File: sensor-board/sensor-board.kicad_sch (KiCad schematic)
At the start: 103 parts, among them J1 USB_C_Receptacle_USB2.0_16P, J10 cap4, J11 header pins, J2 aux pwr, J3 SWD, J4 water 1, J5 water 2, J6 relay, J7 cap1, J8 cap2, J9 cap3, K1 SIL03-1A72-71D, Q1 Si2312, Q2 Si2312, SW1 SW_Push, U1 MLPF-WB55-01E3, U10 EKMB130711, U11 DRV5032, U2 STM32WB55CCUx, U3 MCP1703Ax-300xxTT, U4 SHT40-AD1F-R2, U5 VL53L1CXV0FY1, U6 TLV4082, U7 CLS16D24-44, U8 LIS2DE12TR, U9 FDC2114RGHR, Y1 32.768KHz, Y2 32MHz

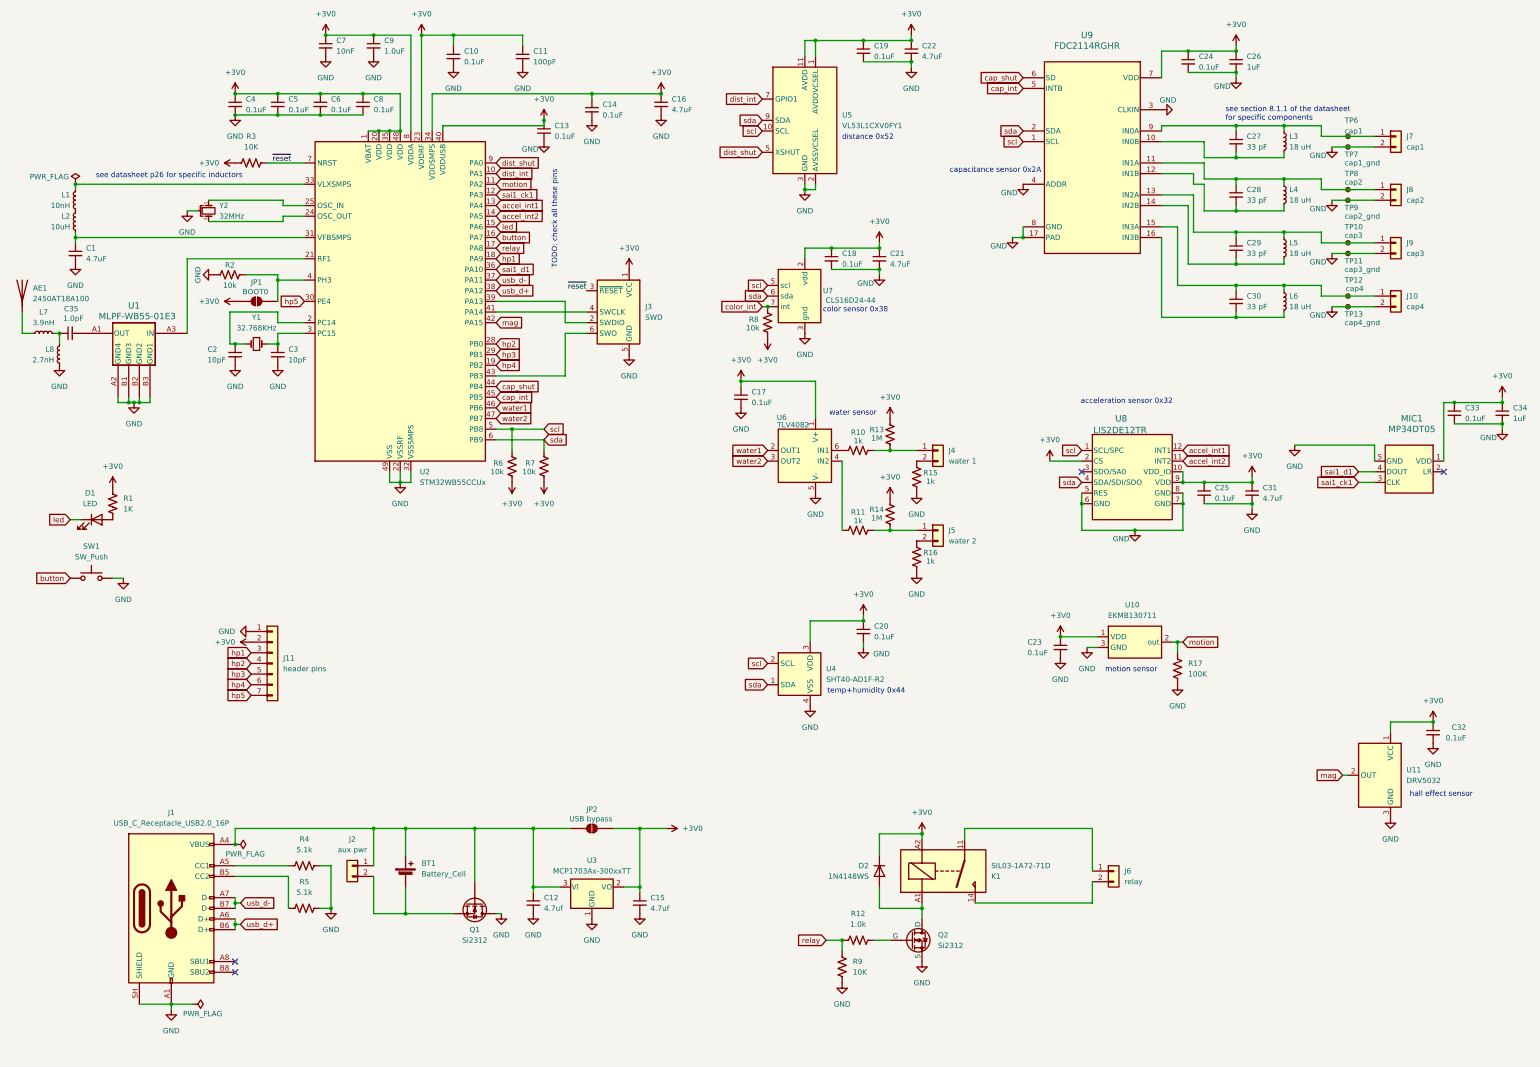
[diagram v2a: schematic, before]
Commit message: Some board grouping, no traces yet
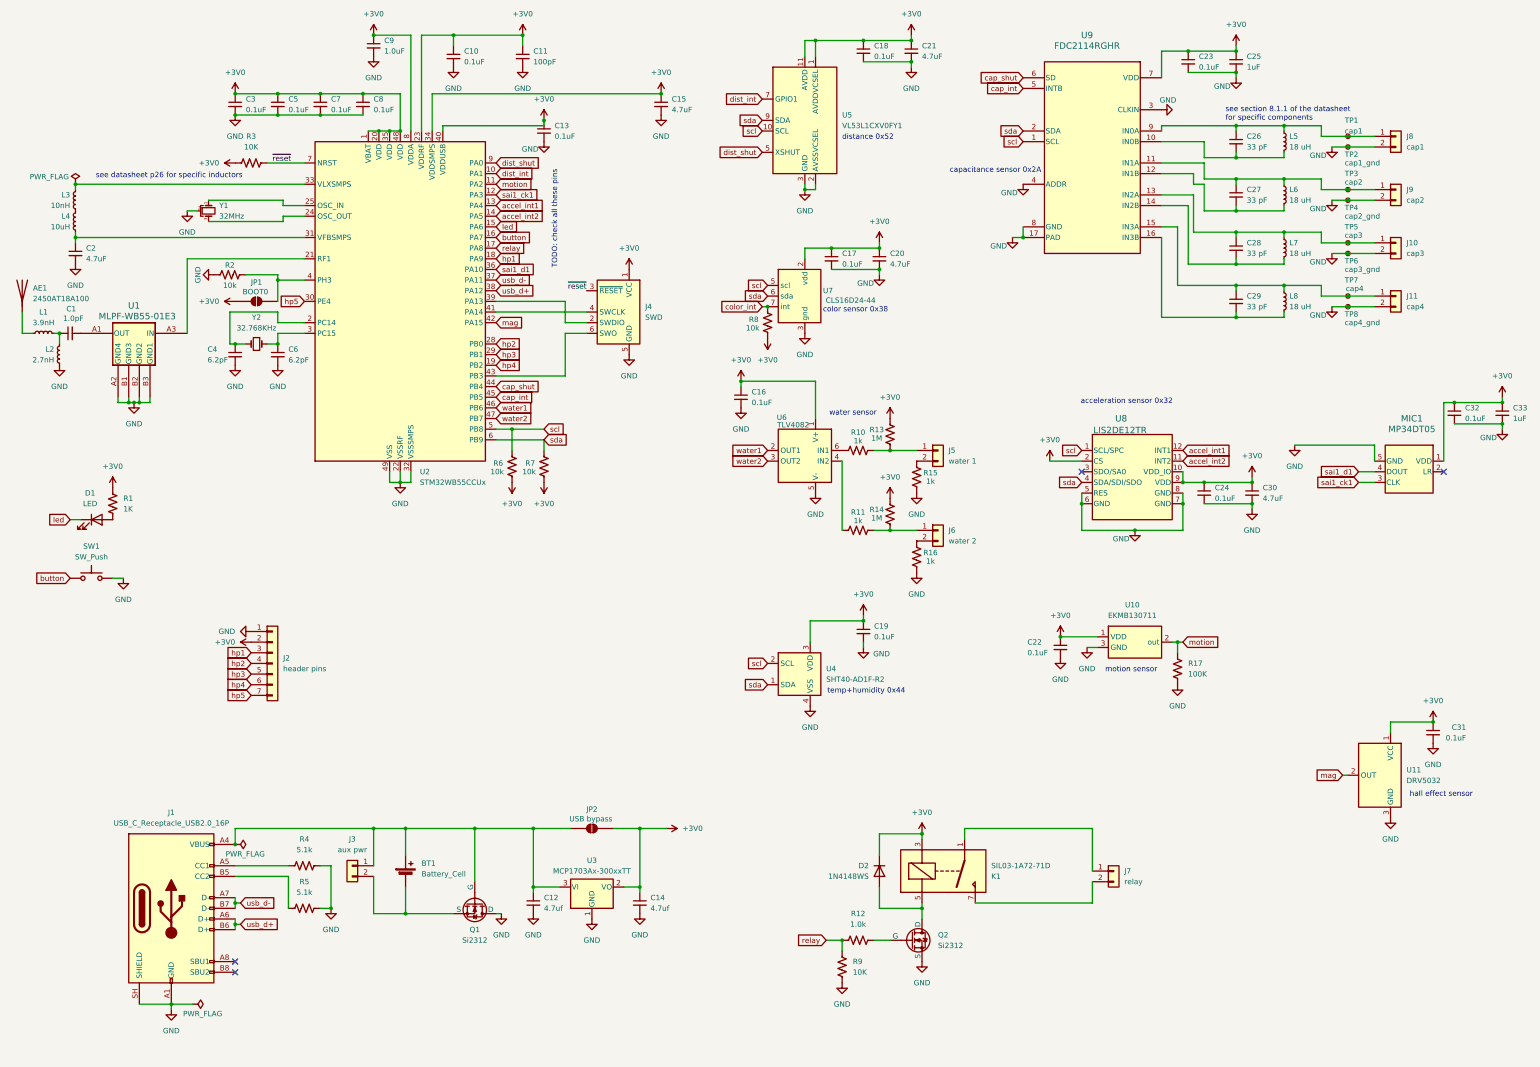
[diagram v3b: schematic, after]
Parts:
- removed C14: 0.1uF, Capacitor_SMD:C_0402_1005Metric, symbol Device:C_Small
- removed C7: 10nF, Capacitor_SMD:C_0402_1005Metric, symbol Device:C_Small
- removed Q1: Si2312, Package_TO_SOT_SMD:SOT-23, symbol Device:Q_NMOS
- added Q1: Si2312, Package_TO_SOT_SMD:SOT-23, symbol Simulation_SPICE:NMOS
- C4: renamed from C2; value 10pF -> 6.2pF
- C6: renamed from C3; value 10pF -> 6.2pF
- renumbered C35 to C1, C15 to C14, C16 to C15, C17 to C16, C18 to C17, C19 to C18, C20 to C19, C1 to C2, C21 to C20, C22 to C21, C23 to C22, C24 to C23, C25 to C24, C26 to C25, C27 to C26, C28 to C27, C29 to C28, C30 to C29, C4 to C3, C31 to C30, C32 to C31, C33 to C32, C34 to C33, C6 to C7, J9 to J10, J10 to J11, J11 to J2, J2 to J3, J3 to J4, J4 to J5, J5 to J6, J6 to J7, J7 to J8, J8 to J9, L7 to L1, L8 to L2, L1 to L3, L2 to L4, L3 to L5, L4 to L6, L5 to L7, L6 to L8, TP6 to TP1, TP7 to TP2, TP8 to TP3, TP9 to TP4, TP10 to TP5, TP11 to TP6, TP12 to TP7, TP13 to TP8, Y2 to Y1, Y1 to Y2
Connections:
- net +3V0: now also K1.3; no longer K1.A2
- net GND: now also Q1.1 (D)
- net at BT1.1 (+), C12.1, J1.A4 (VBUS)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: now also Q1.2 (G)
- net at D2.2 (A), Q2.1 (D): now also K1.5; no longer K1.A1
- net at J7.1 (Pin_1): now also K1.1; no longer K1.11
- net at J7.2 (Pin_2): now also K1.7; no longer K1.14
- net at BT1.2 (-), J3.2 (Pin_2): now also Q1.3 (S)

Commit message: Starting a little bit of routing; starting with HF crystal
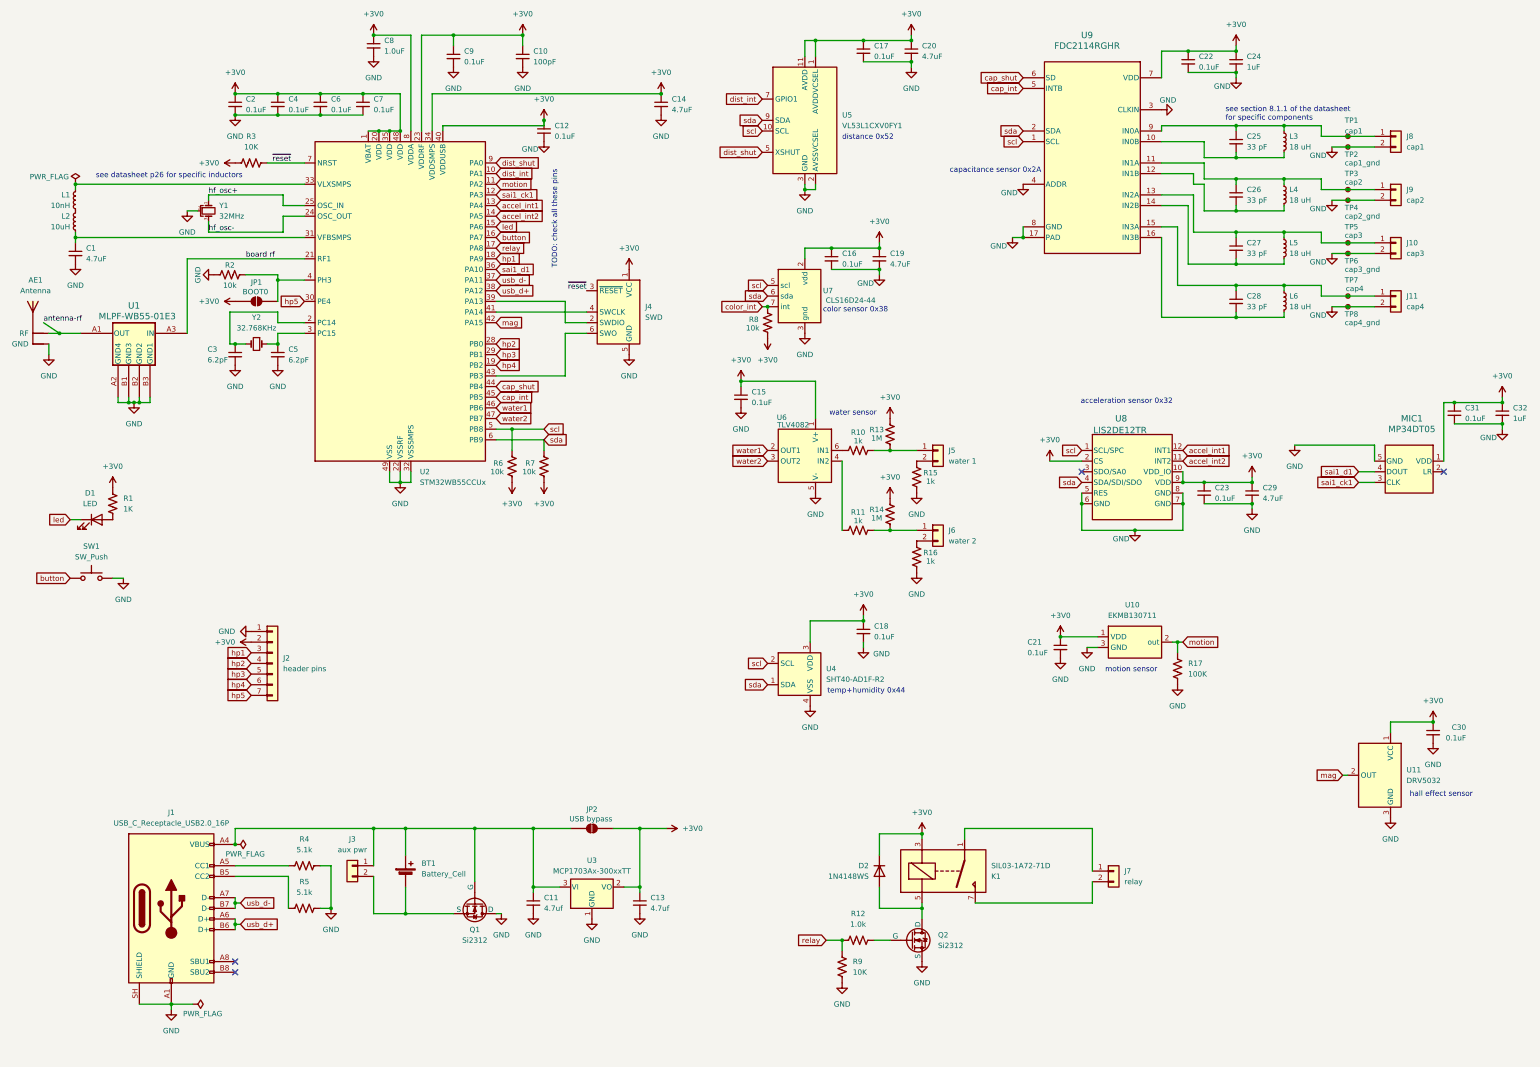
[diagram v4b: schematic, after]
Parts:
- removed C1: 1.0pF, Capacitor_SMD:C_0402_1005Metric, symbol Device:C_Small
- removed L1: 3.9nH, Inductor_SMD:L_0402_1005Metric, symbol Device:L_Small
- removed L2: 2.7nH, Inductor_SMD:L_0402_1005Metric, symbol Device:L_Small
- AE1: value 2450AT18A100 -> Antenna; footprint vendor:XDCR_ACAG0801-2450-T -> vendor:Antenna_2.4GHz_InvertedF_SiLabs; symbol Device:Antenna -> vendor:Antenna_InvertedF
- BT1: footprint (none) -> vendor:BatteryHolder_CR2032
- renumbered C2 to C1, C11 to C10, C12 to C11, C13 to C12, C14 to C13, C15 to C14, C16 to C15, C17 to C16, C18 to C17, C19 to C18, C20 to C19, C3 to C2, C21 to C20, C22 to C21, C23 to C22, C24 to C23, C25 to C24, C26 to C25, C27 to C26, C28 to C27, C29 to C28, C30 to C29, C4 to C3, C31 to C30, C32 to C31, C33 to C32, C5 to C4, C6 to C5, C7 to C6, C8 to C7, C9 to C8, C10 to C9, L3 to L1, L4 to L2, L5 to L3, L6 to L4, L7 to L5, L8 to L6
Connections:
- net GND: now also AE1.2 (GND)
- net antenna-rf: now reaches U1.A1 (OUT)
- net antenna-rf: now also AE1.1 (RF)
- net board rf: now reaches U1.A3 (IN), U2.21 (RF1)
- net hf_osc-: now reaches U2.24 (OSC_OUT), Y1.3
- net hf_osc+: now reaches U2.25 (OSC_IN), Y1.1

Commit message: SMPS and (most of) LF crystal
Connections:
- net lf_osc-: now reaches C5.1, U2.3 (PC15), Y2.1
- net lf_osc+: now reaches C3.1, U2.2 (PC14), Y2.2
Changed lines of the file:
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@@
 	)
 	(junction
-		(at 29.21 54.61)
-		(diameter 0)
-		(color 0 0 0 0)
-	)
-	(junction
 		(at 306.07 73.66)
 		(diameter 0)
@@
 	)
 	(junction
+		(at 29.21 54.61)
+		(diameter 0)
+		(color 0 0 0 0)
+	)
+	(junction
 		(at 332.74 43.18)
 		(diameter 0)
@@
 	(wire
 		(pts
+			(xy 29.21 52.07) (xy 29.21 54.61)
+		)
+		(stroke
+			(width 0)
+			(type default)
+		)
+	)
+	(wire
+		(pts
 			(xy 29.21 68.58) (xy 29.21 67.31)
 		)
@@
 		)
 	)
+	(label "lf_osc+"
+		(at 77.47 87.63 0)
+		(effects
+			(font
+				(size 1.27 1.27)
+			)
+			(justify left bottom)
+		)
+	)
 	(label "~{reset}"
 		(at 76.2 49.53 0)
@@
 		)
 	)
+	(label "lf_osc-"
+		(at 77.47 90.17 0)
+		(effects
+			(font
+				(size 1.27 1.27)
+			)
+			(justify left bottom)
+		)
+	)
 	(global_label "hp4"
 		(shape input)
@@
 	(symbol
 		(lib_id "power:PWR_FLAG")
-		(at 29.21 54.61 0)
+		(at 29.21 52.07 0)
 		(unit 1)
 		(body_style 1)
@@
 		(dnp no)
 		(property "Reference" "#FLG01"
-			(at 29.21 52.705 0)
+			(at 29.21 50.165 0)
 			(hide yes)
 			(show_name no)
@@
 		)
 		(property "Value" "PWR_FLAG"
-			(at 18.288 52.832 0)
+			(at 18.288 50.292 0)
 			(show_name no)
 			(do_not_autoplace no)
@@
 		)
 		(property "Footprint" ""
-			(at 29.21 54.61 0)
+			(at 29.21 52.07 0)
 			(hide yes)
 			(show_name no)
@@
 		)
 		(property "Datasheet" ""
-			(at 29.21 54.61 0)
+			(at 29.21 52.07 0)
 			(hide yes)
 			(show_name no)
@@
 		)
 		(property "Description" "Special symbol for telling ERC where power comes from"
-			(at 29.21 54.61 0)
+			(at 29.21 52.07 0)
 			(hide yes)
 			(show_name no)

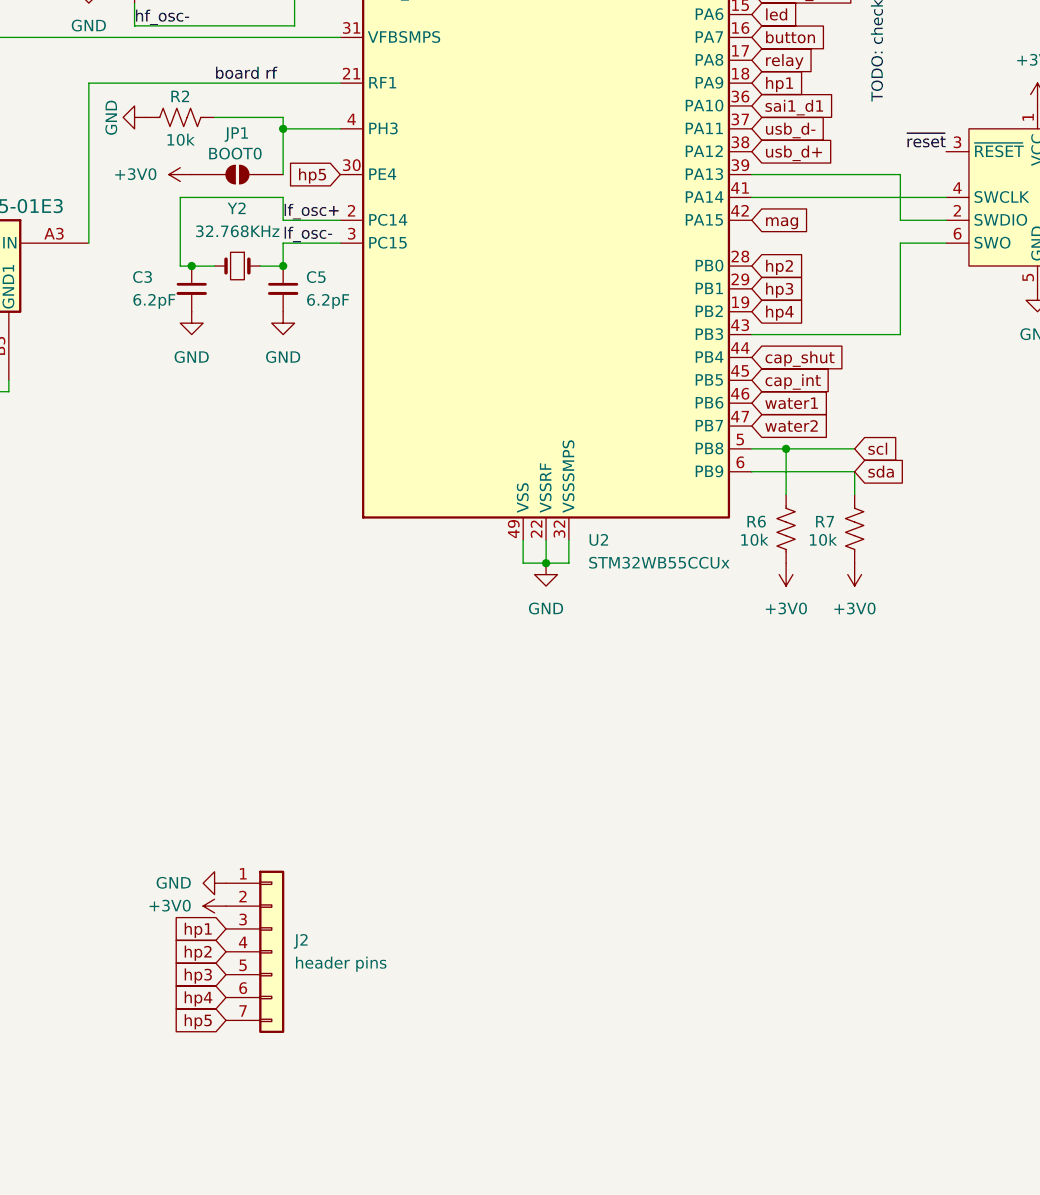
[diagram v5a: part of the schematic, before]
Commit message: ~Finished routing, not yet DRC-clean
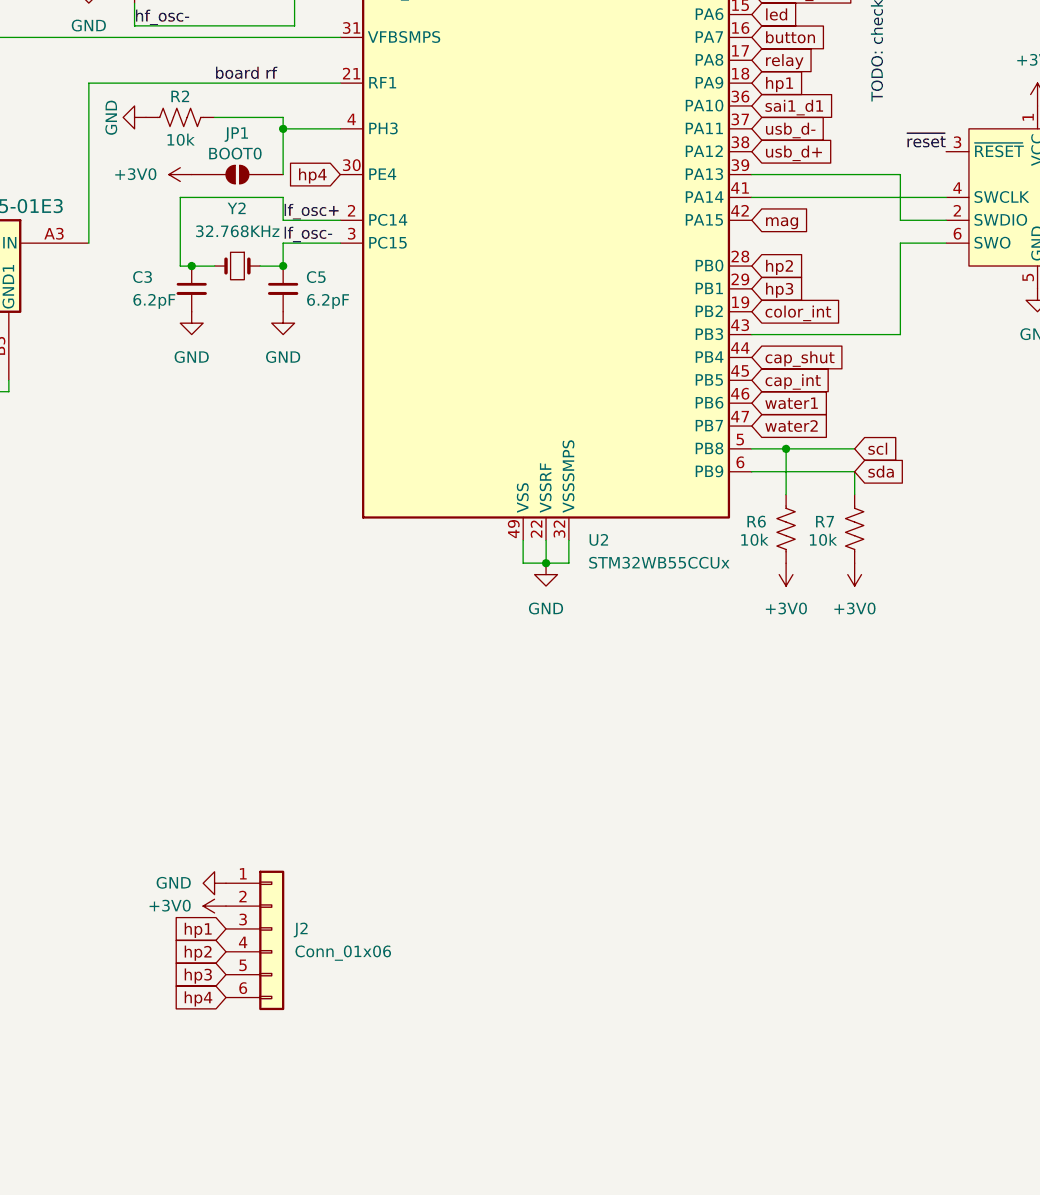
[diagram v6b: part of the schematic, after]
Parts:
- removed J2: header pins, Connector_PinHeader_2.54mm:PinHeader_1x07_P2.54mm_Vertical, symbol Connector_Generic:Conn_01x07
- added J2: Conn_01x06, Connector_PinHeader_2.54mm:PinHeader_1x06_P2.54mm_Vertical, symbol Connector_Generic:Conn_01x06
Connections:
- net hp5 is gone; now on net hp4: U2.30 (PE4)
- net +3V0: now also J2.2 (Pin_2)
- net GND: now also J2.1 (Pin_1)
- net color_int: now also U2.19 (PB2)
- net hp1: now also J2.3 (Pin_3)
- net hp2: now also J2.4 (Pin_4)
- net hp3: now also J2.5 (Pin_5)
- net hp4: now also J2.6 (Pin_6); no longer U2.19 (PB2)

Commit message: Address some human-discovered issues
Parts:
- added R18: 2.2M, Resistor_SMD:R_0603_1608Metric, symbol Device:R_US
- added R19: 1.0k, Resistor_SMD:R_0402_1005Metric, symbol Device:R_US
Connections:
- net GND: now also Q1.3 (S), R18.2; no longer Q1.1 (D)
- net at BT1.1 (+), C11.1, J1.A4 (VBUS)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: now also R18.1, R19.2; no longer Q1.2 (G)
- net at BT1.2 (-), J3.2 (Pin_2): now also Q1.1 (D); no longer Q1.3 (S)
- new net: Q1.2 (G), R19.1
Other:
- note added: "CR nausicaa: i realized today that this guy was backwards (does have a diode, which will conduct (incorrectly) on rev. polarity, and also realized that we should pull the source to the gate to ensure this fella stays off. Cgs ≈ 668 pF, Rg = 2 MΩ gives a time constant of around 1.5 ms, which should be short enough to not hurt anybody, and draws about 1.5 μA while on."
- note added: "CR nausicaa: i wonder if we want series resistors ahead of water* to limit slew rate somewhat."
- moved on the sheet: C11, C13, JP2, Q1, U3
